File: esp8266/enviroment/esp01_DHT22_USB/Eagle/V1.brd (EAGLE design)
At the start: 59.7 x 31.4 mm, 13 parts, among them IC1 LD117AV33, X1 MINI-USB_4P-85-32004-10X

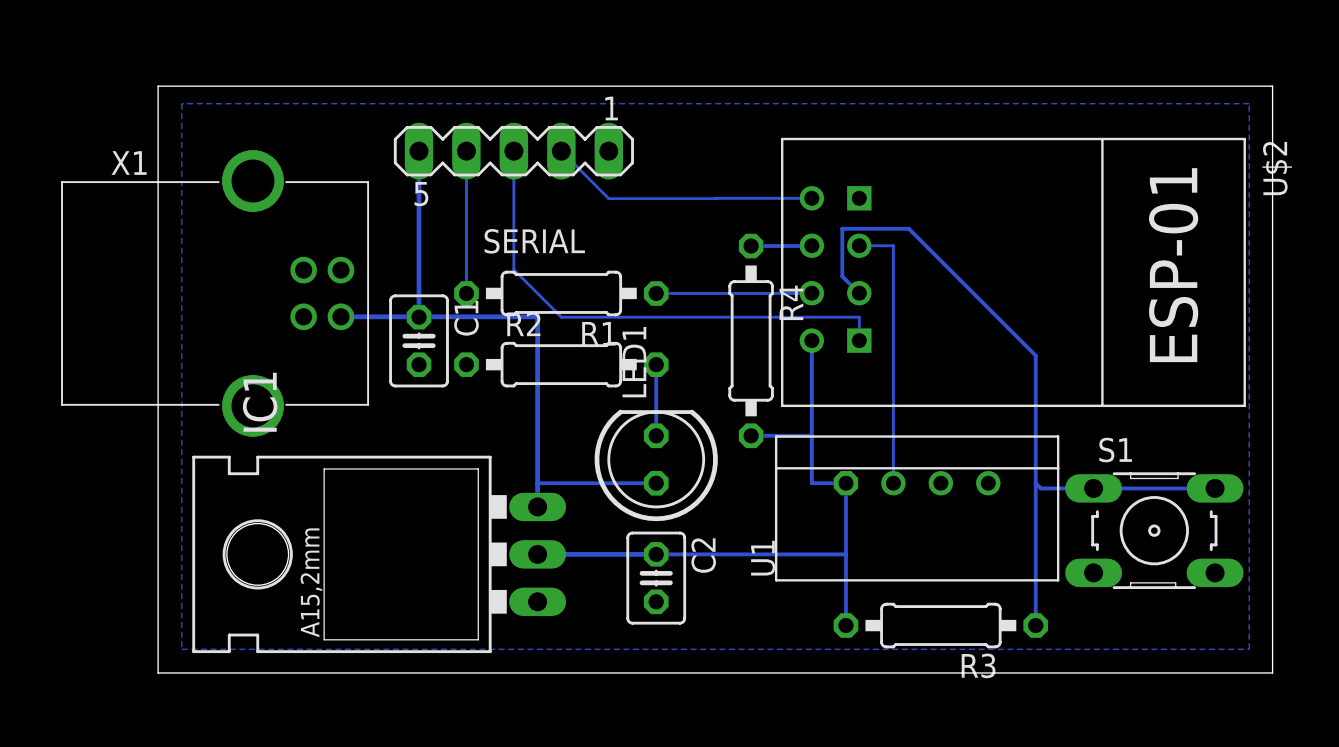
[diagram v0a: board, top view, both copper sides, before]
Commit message: Changed Programmer-Pinout
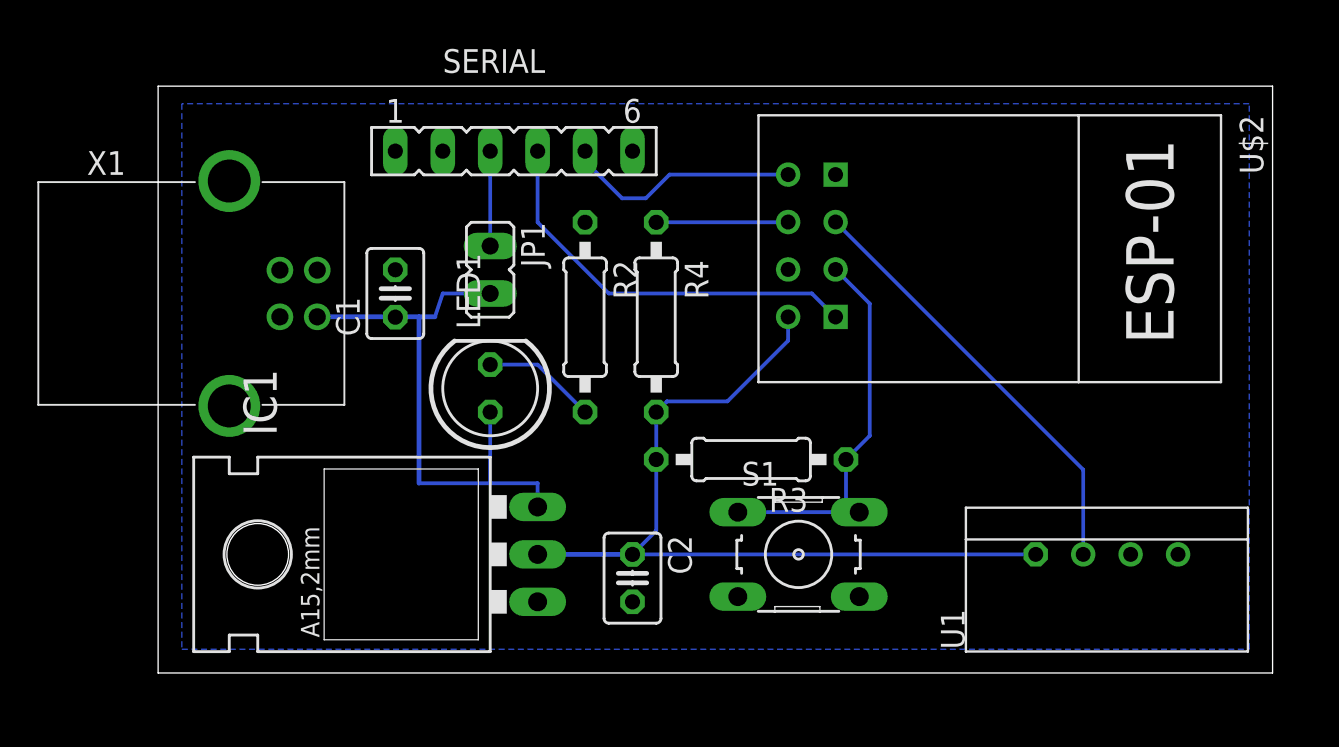
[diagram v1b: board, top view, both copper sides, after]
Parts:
- removed R1: 10k, rcl:0207/10
- added JP1: (no value), jumper:JP1
- SERIAL: device con-lstb:MA05-1 -> con-lsta:FE06
- moved S1 19.1 mm to (34.3, 76.2)
- moved R3 13.5 mm to (31.8, 81.3)
- moved U1 10.9 mm to (50.8, 76.2)
- moved LED1 9.67 mm to (17.8, 85.1)
- moved R4 5.24 mm to (26.7, 88.9)
- moved C1 2.84 mm to (12.7, 90.2), turned to 90 degrees
- moved R2 2.84 mm to (22.9, 88.9), turned to 270 degrees
- moved U$2 1.80 mm to (41.9, 92.7)
- moved C2 1.27 mm to (25.4, 74.9)
- moved X1 1.27 mm to (3.81, 90.2)
- turned SERIAL to 0 degrees
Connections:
- removed net RESET: R1.2, SERIAL.4
- net 5V: now also JP1.2; no longer SERIAL.5
- net N$1: now also JP1.1, SERIAL.3; no longer R1.1, U$2.RST
- net RXD: now also SERIAL.4; no longer SERIAL.3
- net TXD: now also SERIAL.5; no longer SERIAL.2
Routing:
- net N$3: track 41.2 -> 20.8 mm
- net DHT_DATA: track 14.5 -> 23.3 mm
- net 3V: track 36.8 -> 44.7 mm
- net RESET: track 7.62 -> 0.00 mm
- net 5V: track 36.0 -> 30.5 mm
- net RXD: track 27.1 -> 21.9 mm
- net N$4: track 3.26 -> 7.07 mm
- net N$1: track 8.34 -> 5.34 mm
- net N$2: track 3.81 -> 6.13 mm
- net TXD: track 14.5 -> 12.8 mm

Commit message: Changed Voltage-Regulator to fit pseudo-standart pinout
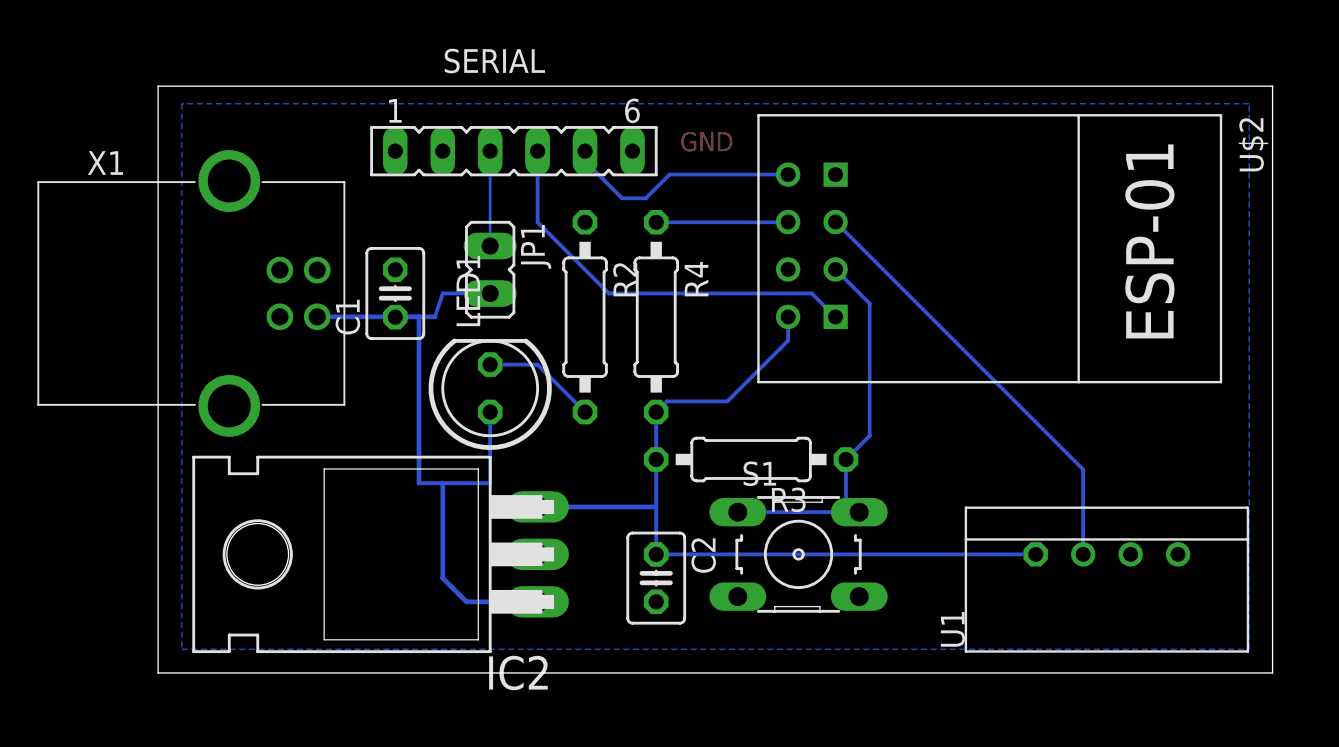
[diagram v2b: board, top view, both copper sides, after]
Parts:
- removed IC1: LD117AV33, v-reg:TO220L1
- added IC2: 7805T, linear:TO220H
- moved C2 1.27 mm to (26.7, 74.9)
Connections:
- net 3V: now also IC2.3; no longer IC1.2
- net 5V: now also IC2.1; no longer IC1.3
- net GND: now also IC2.2; no longer IC1.1
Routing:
- net 5V: track 30.5 -> 37.4 mm
- net 3V: track 44.7 -> 44.2 mm
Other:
- board text added: "GND"
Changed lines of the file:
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@@
 <?xml version="1.0" encoding="utf-8"?>
 <!DOCTYPE eagle SYSTEM "eagle.dtd">
-<eagle version="9.2.1">
+<eagle version="9.2.2">
 <drawing>
 <settings>
@@
 <layer number="21" name="tPlace" color="7" fill="1" visible="yes" active="yes"/>
 <layer number="22" name="bPlace" color="7" fill="1" visible="yes" active="yes"/>
-<layer number="23" name="tOrigins" color="15" fill="1" visible="yes" active="yes"/>
-<layer number="24" name="bOrigins" color="15" fill="1" visible="yes" active="yes"/>
-<layer number="25" name="tNames" color="7" fill="1" visible="yes" active="yes"/>
-<layer number="26" name="bNames" color="7" fill="1" visible="yes" active="yes"/>
-<layer number="27" name="tValues" color="7" fill="1" visible="yes" active="yes"/>
-<layer number="28" name="bValues" color="7" fill="1" visible="yes" active="yes"/>
+<layer number="23" name="tOrigins" color="15" fill="1" visible="no" active="yes"/>
+<layer number="24" name="bOrigins" color="15" fill="1" visible="no" active="yes"/>
+<layer number="25" name="tNames" color="7" fill="1" visible="no" active="yes"/>
+<layer number="26" name="bNames" color="7" fill="1" visible="no" active="yes"/>
+<layer number="27" name="tValues" color="7" fill="1" visible="no" active="yes"/>
+<layer number="28" name="bValues" color="7" fill="1" visible="no" active="yes"/>
 <layer number="29" name="tStop" color="7" fill="3" visible="no" active="yes"/>
 <layer number="30" name="bStop" color="7" fill="6" visible="no" active="yes"/>
@@
 <wire x1="59.67" y1="101.27" x2="0" y2="101.27" width="0" layer="20"/>
 <wire x1="0" y1="101.27" x2="0" y2="69.85" width="0" layer="20"/>
+<text x="27.94" y="97.79" size="1.016" layer="1">GND</text>
 </plain>
 <attributes>
@@
 <attribute name="VALUE" x="-4.445" y="91.44" size="1.27" layer="27"/>
 </element>
-<element name="IC1" library="v-reg" library_urn="urn:adsk.eagle:library:409" package="TO220L1" package3d_urn="urn:adsk.eagle:package:30365/1" value="LD117AV33" x="16.51" y="76.2" smashed="yes" rot="R90">
-<attribute name="NAME" x="6.35" y="82.55" size="1.778" layer="25" ratio="10" rot="R90"/>
-<attribute name="VALUE" x="7.62" y="81.153" size="1.778" layer="27" ratio="10" rot="R90"/>
-</element>
 <element name="C1" library="rcl" library_urn="urn:adsk.eagle:library:334" package="C025-030X050" package3d_urn="urn:adsk.eagle:package:23631/1" value="100nF" x="12.7" y="90.17" smashed="yes" rot="R90">
 <attribute name="NAME" x="10.795" y="87.884" size="1.27" layer="25" ratio="10" rot="R90"/>
@@
 <attribute name="VALUE" x="13.208" y="94.234" size="1.27" layer="27" ratio="10" rot="R90"/>
 </element>
-<element name="C2" library="rcl" library_urn="urn:adsk.eagle:library:334" package="C025-030X050" package3d_urn="urn:adsk.eagle:package:23631/1" value="10uF" x="25.4" y="74.93" smashed="yes" rot="R270">
-<attribute name="NAME" x="27.305" y="77.216" size="1.27" layer="25" ratio="10" rot="R270"/>
-<attribute name="SPICEPREFIX" value="C" x="25.4" y="74.93" size="1.778" layer="27" rot="R270" display="off"/>
-<attribute name="VALUE" x="22.352" y="77.216" size="1.27" layer="27" ratio="10" rot="R270"/>
+<element name="C2" library="rcl" library_urn="urn:adsk.eagle:library:334" package="C025-030X050" package3d_urn="urn:adsk.eagle:package:23631/1" value="10uF" x="26.67" y="74.93" smashed="yes" rot="R270">
+<attribute name="NAME" x="28.575" y="77.216" size="1.27" layer="25" ratio="10" rot="R270"/>
+<attribute name="SPICEPREFIX" value="C" x="26.67" y="74.93" size="1.778" layer="27" rot="R270" display="off"/>
+<attribute name="VALUE" x="23.622" y="77.216" size="1.27" layer="27" ratio="10" rot="R270"/>
 </element>
 <element name="SERIAL" library="con-lsta" library_urn="urn:adsk.eagle:library:161" package="FE06" package3d_urn="urn:adsk.eagle:package:8191/1" value="H1" x="19.05" y="97.79" smashed="yes">
@@
 <attribute name="VALUE" x="14.859" y="93.98" size="1.27" layer="27" ratio="10" rot="R270"/>
 </element>
+<element name="IC2" library="linear" library_urn="urn:adsk.eagle:library:262" package="TO220H" package3d_urn="urn:adsk.eagle:package:16414/1" value="7805T" x="10.16" y="76.2" smashed="yes" rot="R90">
+<attribute name="NAME" x="21.082" y="70.739" size="1.778" layer="25" ratio="10" rot="R180"/>
+<attribute name="VALUE" x="21.209" y="83.566" size="1.778" layer="27" ratio="10" rot="R180"/>
+</element>
 </elements>
 <signals>
@@
 <contactref element="X1" pad="4"/>
 <contactref element="U$2" pad="GND"/>
-<contactref element="IC1" pad="1"/>
 <contactref element="C1" pad="2"/>
 <contactref element="C2" pad="2"/>
@@
 <contactref element="S1" pad="4"/>
 <contactref element="S1" pad="3"/>
+<contactref element="IC2" pad="2"/>
 </signal>
 <signal name="5V">
 <contactref element="X1" pad="1"/>
-<contactref element="IC1" pad="3"/>
 <contactref element="C1" pad="1"/>
 <wire x1="14.823334375" y1="88.92" x2="13.97" y2="88.92" width="0.254" layer="16"/>
@@
 <wire x1="13.97" y1="80.01" x2="13.97" y2="88.92" width="0.254" layer="16"/>
 <contactref element="JP1" pad="2"/>
-<wire x1="20.32" y1="80.01" x2="17.78" y2="80.01" width="0.2032" layer="16"/>
-<wire x1="17.78" y1="80.01" x2="13.97" y2="80.01" width="0.2032" layer="16"/>
-<wire x1="20.32" y1="78.74" x2="20.32" y2="80.01" width="0.2032" layer="16"/>
+<wire x1="17.78" y1="80.01" x2="15.24" y2="80.01" width="0.2032" layer="16"/>
+<wire x1="15.24" y1="80.01" x2="13.97" y2="80.01" width="0.2032" layer="16"/>
 <wire x1="17.78" y1="80.01" x2="17.78" y2="83.82" width="0.2032" layer="16"/>
 <wire x1="15.24" y1="90.17" x2="17.78" y2="90.17" width="0.2032" layer="16"/>
 <wire x1="15.24" y1="90.17" x2="14.823334375" y2="88.92" width="0.2032" layer="16"/>
 <wire x1="12.7" y1="88.9" x2="12.7" y2="88.92" width="0.2032" layer="16"/>
+<contactref element="IC2" pad="1"/>
+<wire x1="20.32" y1="73.66" x2="16.51" y2="73.66" width="0.254" layer="16"/>
+<wire x1="16.51" y1="73.66" x2="15.24" y2="74.93" width="0.254" layer="16"/>
+<wire x1="15.24" y1="74.93" x2="15.24" y2="80.01" width="0.254" layer="16"/>
 </signal>
 <signal name="3V">
 <contactref element="U$2" pad="VCC"/>
-<contactref element="IC1" pad="2"/>
 <contactref element="C2" pad="1"/>
 <contactref element="U1" pad="VDD"/>
-<wire x1="20.32" y1="76.2" x2="25.4" y2="76.2" width="0.254" layer="16"/>
 <contactref element="R3" pad="2"/>
-<wire x1="26.67" y1="81.28" x2="26.67" y2="77.47" width="0.2032" layer="16"/>
-<wire x1="26.67" y1="77.47" x2="25.4" y2="76.2" width="0.2032" layer="16"/>
+<wire x1="26.67" y1="81.28" x2="26.67" y2="78.74" width="0.2032" layer="16"/>
 <contactref element="R4" pad="2"/>
+<wire x1="26.67" y1="78.74" x2="26.67" y2="76.2" width="0.2032" layer="16"/>
 <wire x1="26.67" y1="83.82" x2="26.67" y2="81.28" width="0.2032" layer="16"/>
 <wire x1="30.48" y1="84.3925" x2="27.2425" y2="84.3925" width="0.2032" layer="16"/>
@@
 <wire x1="33.7325" y1="87.645" x2="33.7325" y2="88.915" width="0.2032" layer="16"/>
 <wire x1="33.7325" y1="87.645" x2="30.48" y2="84.3925" width="0.2032" layer="16"/>
-<wire x1="25.4" y1="76.2" x2="46.99" y2="76.2" width="0.2032" layer="16"/>
+<wire x1="26.67" y1="76.2" x2="46.99" y2="76.2" width="0.2032" layer="16"/>
+<contactref element="IC2" pad="3"/>
+<wire x1="20.32" y1="78.74" x2="26.67" y2="78.74" width="0.254" layer="16"/>
 </signal>
 <signal name="RXD">
@@
 <contactref element="SERIAL" pad="3"/>
 <contactref element="JP1" pad="1"/>
-<wire x1="17.78" y1="96.7105" x2="17.526" y2="96.774" width="0.2032" layer="16"/>
-<wire x1="17.78" y1="97.79" x2="17.78" y2="92.71" width="0.2032" layer="16"/>
-<wire x1="17.78" y1="97.79" x2="17.526" y2="96.774" width="0" layer="19" extent="16-16"/>
+<wire x1="17.78" y1="97.79" x2="17.78" y2="92.71" width="0.1524" layer="16"/>
 </signal>
 </signals>
